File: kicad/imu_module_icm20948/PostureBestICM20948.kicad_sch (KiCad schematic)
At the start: 11 parts, among them J1 I2C/VDCG, SW1 SW_SPDT, U1 ICM-20948, U2 AMS1117-1.8

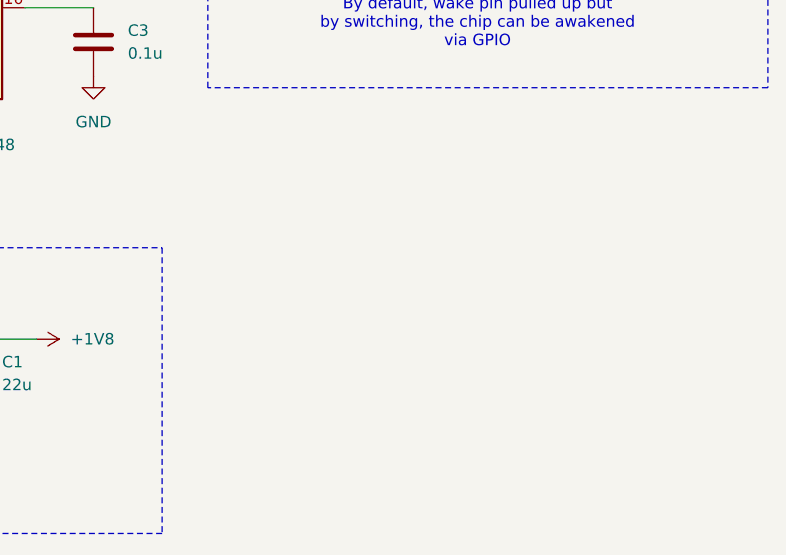
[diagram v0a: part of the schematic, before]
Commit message: added missing power traces
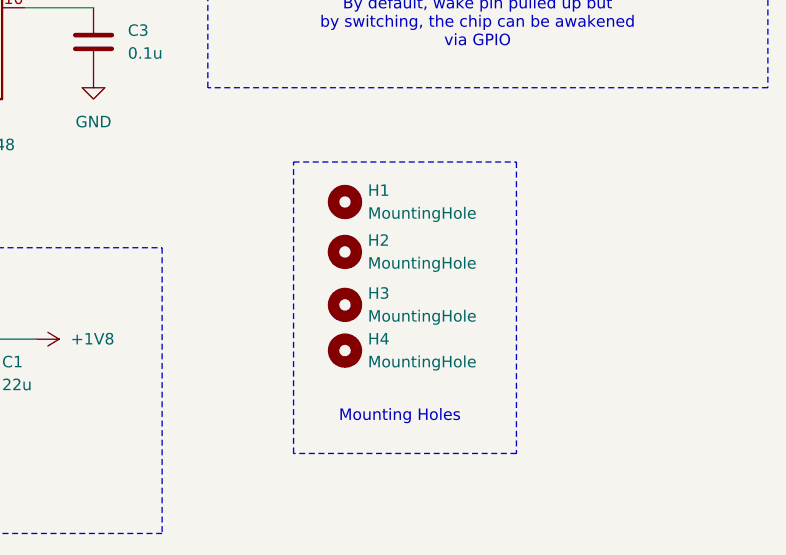
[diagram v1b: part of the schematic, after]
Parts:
- added H1, H2, H3, H4: MountingHole, MountingHole:MountingHole_2.2mm_M2, symbol Mechanical:MountingHole
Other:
- note added: "Mounting Holes"
